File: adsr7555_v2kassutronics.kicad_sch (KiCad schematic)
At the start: 47 parts, among them J1 Power, J2 GateIn, J5 Atn Out, J6 Output, Q1 3904, Q2 3904, Q3 3904, Q4 3904, SW1 SW_Push, U1 7555, U2 TL074

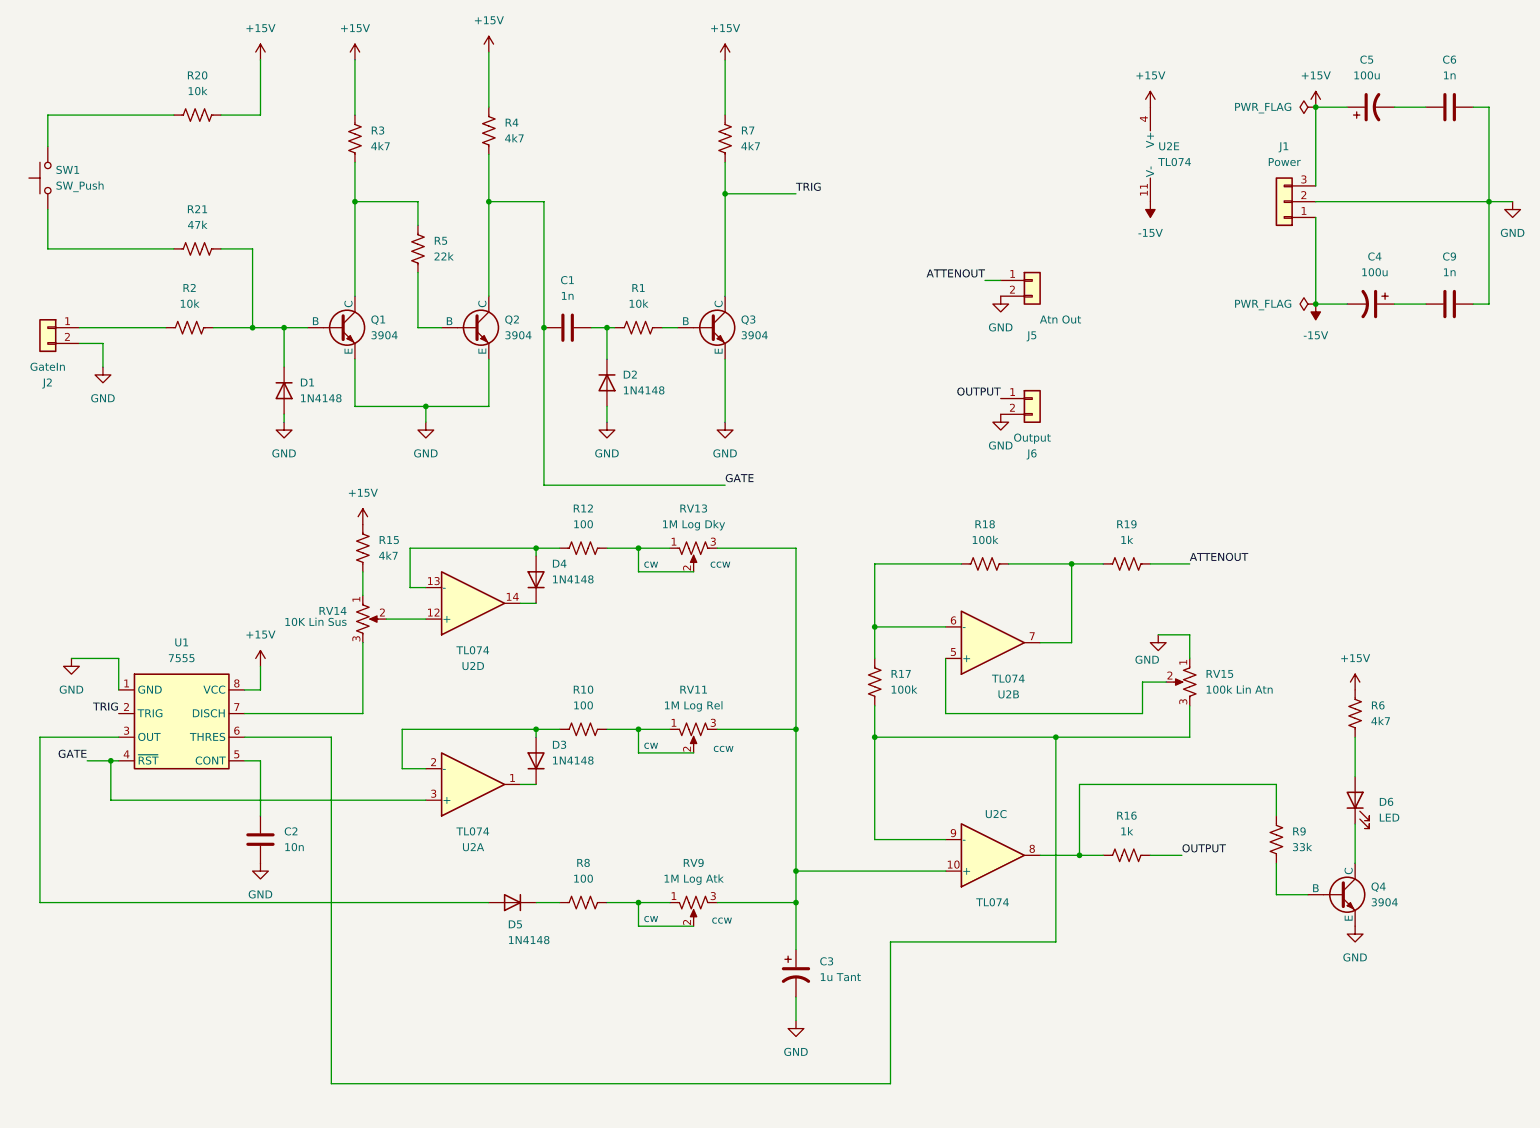
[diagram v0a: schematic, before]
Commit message: archived v1 to jail. Redo for v2
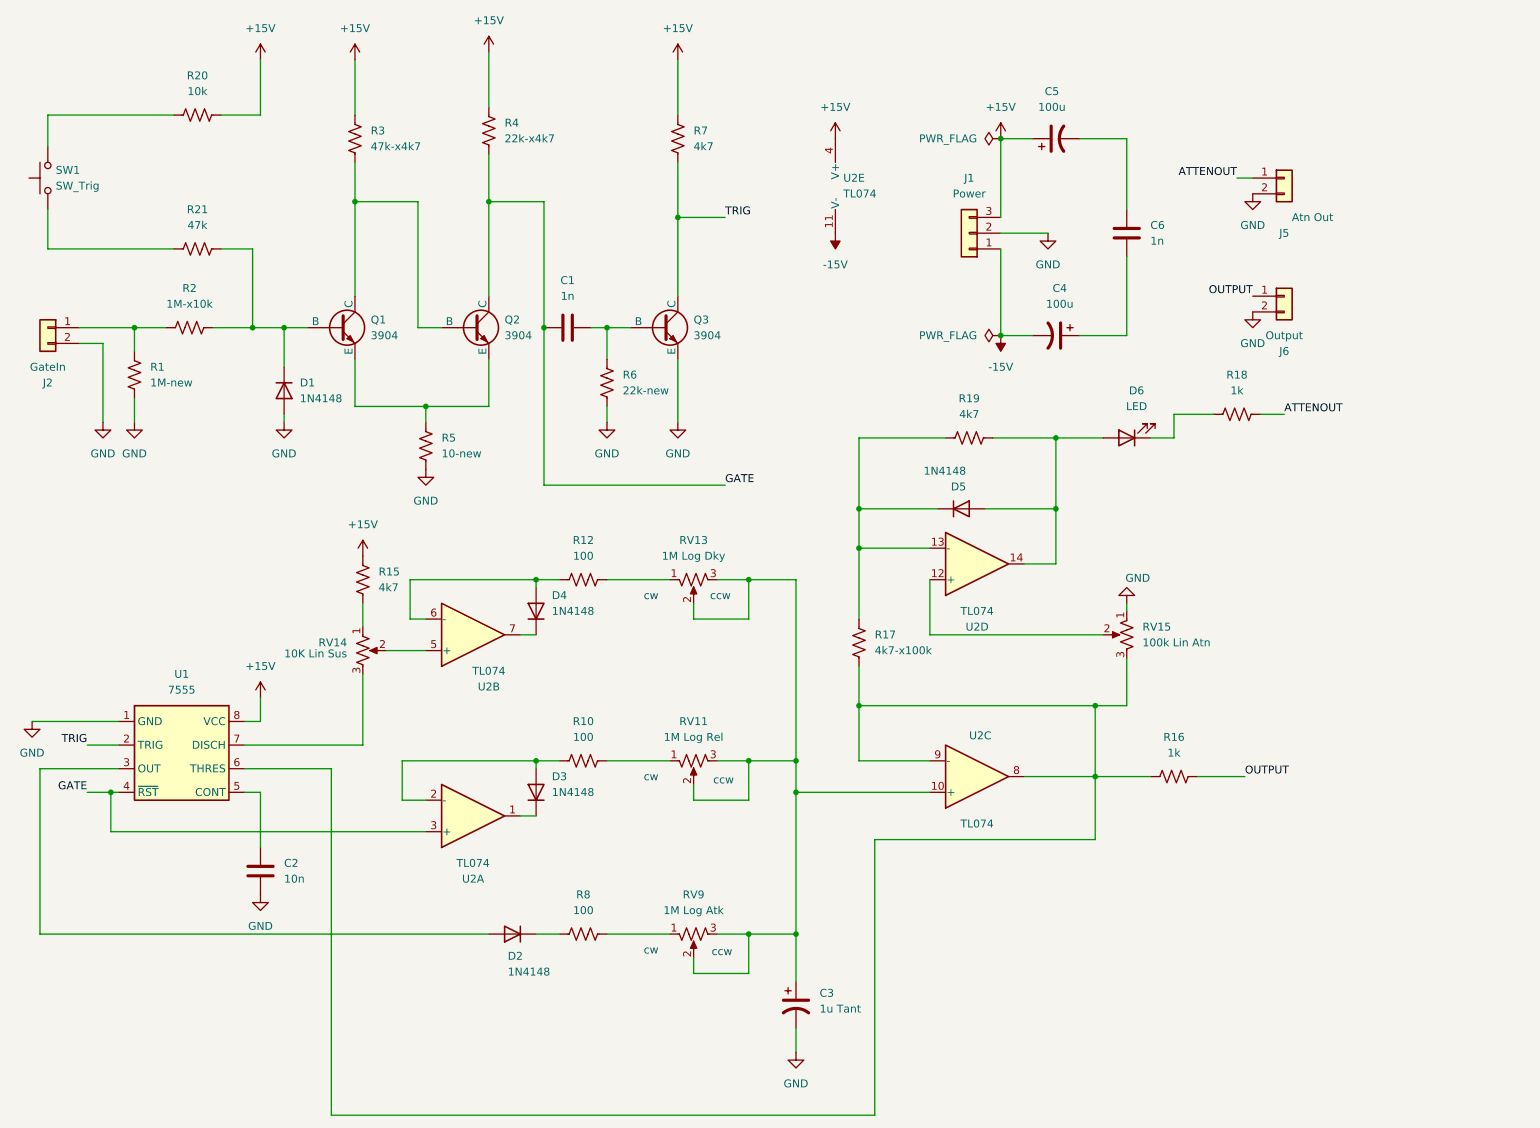
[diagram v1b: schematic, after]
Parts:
- removed C9: 1n, Capacitor_THT:C_Disc_D4.7mm_W2.5mm_P5.00mm, symbol Device:C
- removed D2: 1N4148, Diode_THT:D_DO-35_SOD27_P7.62mm_Horizontal, symbol Diode:1N4148
- removed Q4: 3904, Package_TO_SOT_THT:TO-92L_Inline_Wide, symbol Simulation_SPICE:NPN
- removed R6: 4k7, Resistor_THT:R_Axial_DIN0204_L3.6mm_D1.6mm_P7.62mm_Horizontal, symbol Device:R_US
- removed R9: 33k, Resistor_THT:R_Axial_DIN0204_L3.6mm_D1.6mm_P7.62mm_Horizontal, symbol Device:R_US
- added D5: 1N4148, Diode_THT:D_DO-35_SOD27_P7.62mm_Horizontal, symbol Diode:1N4148
- added R1: 1M-new, Resistor_THT:R_Axial_DIN0204_L3.6mm_D1.6mm_P7.62mm_Horizontal, symbol Device:R_US
- R17: value 100k -> 4k7-x100k
- R19: renamed from R18; value 100k -> 4k7
- R2: value 10k -> 1M-x10k
- R3: value 4k7 -> 47k-x4k7
- R4: value 4k7 -> 22k-x4k7
- R5: value 22k -> 10-new
- R6: renamed from R1; value 10k -> 22k-new
- SW1: value SW_Push -> SW_Trig
- renumbered D5 to D2, R19 to R18
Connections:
- net GND: now also R5.1, R6.1, R1.1; no longer C6.2, Q1.3 (E), Q2.3 (E)
- net at R17.1, RV15.3, U1.6 (THRES)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: now also R16.2, U2.8
- net at RV15.2: now also U2.12 (+); no longer U2.5 (+)
- net at D6.1 (K): now also R18.2
- net at R10.2, RV11.1: no longer RV11.2
- net at C3.1, RV11.3, RV13.3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: now also RV11.2, RV13.2, RV9.2
- net at Q1.1 (C), R3.1: now also Q2.2 (B); no longer R5.2
- net at C1.2: now also Q3.2 (B), R6.2; no longer R6.1
- net at C5.2: now also C6.2; no longer C6.1
- net at RV14.2: now also U2.5 (+); no longer U2.12 (+)
- net at D4.2 (A), R12.1: now also U2.6 (-); no longer U2.13 (-)
- net at U2.14: now also D6.2 (A), R19.1, D5.2 (A); no longer D4.1 (K)
- net at R17.2, R19.2: now also U2.13 (-), D5.1 (K); no longer U2.6 (-)
- net at J2.1 (Pin_1), R2.1: now also R1.2
- net at R12.2, RV13.1: no longer RV13.2
- net at R8.2, RV9.1: no longer RV9.2
- net at C4.1: now also C6.1
- new net: Q1.3 (E), Q2.3 (E), R5.2
- new net: D4.1 (K), U2.7
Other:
- moved on the sheet: C2, C3, C4, C5, D2, D3, D4, D6, J1, J5, J6, Q3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

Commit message: added pdfs for sch and pcb
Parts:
- removed RV15: 100k Lin Atn, Potentiometer_THT:Potentiometer_Bourns_3296W_Vertical, symbol Device:R_Potentiometer_US
- R7: value 4k7 -> 22k-x4k7
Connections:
- net GND: now also U2.12 (+)
- net THR: now reaches R16.2, R17.1, U1.6 (THRES), U2.8, U2.9 (-)
- net ATTENOUT renamed INVOUT
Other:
- title: Kassutronics Precision ADSR -> Kassutronics Precision ADSR V2

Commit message: revised SCH from Bergman
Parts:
- R1: value 1M-new -> 1M
- R17: value 4k7-x100k -> 4k7
- R3: value 47k-x4k7 -> 47k
- R4, R7: value 22k-x4k7 -> 22k
- R5: value 10-new -> 10
- R6: value 22k-new -> 22k
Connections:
- net +15V: now also C6.2; no longer J1.3 (Pin_3)
- net -15V: now also C6.1; no longer J1.1 (Pin_1)
- net at C5.2: now also J1.3 (Pin_3); no longer C6.2
- net at C4.1: now also J1.1 (Pin_1); no longer C6.1
- net INVOUT: no longer names the net of J5.1 (Pin_1), R18.1
- net OUTPUT: no longer names the net of J6.1 (Pin_1), R16.1
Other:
- moved on the sheet: C4, C5, C6, J1, J5, J6, U2E

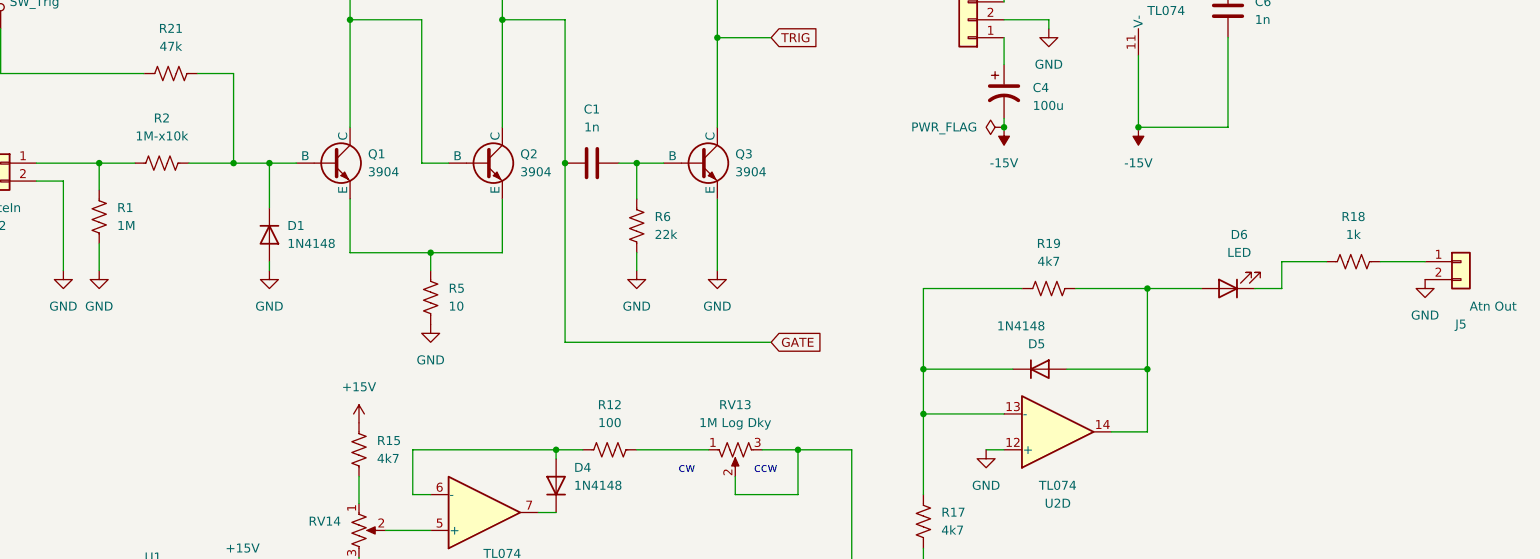
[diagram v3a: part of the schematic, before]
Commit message: modified wiring on U2D
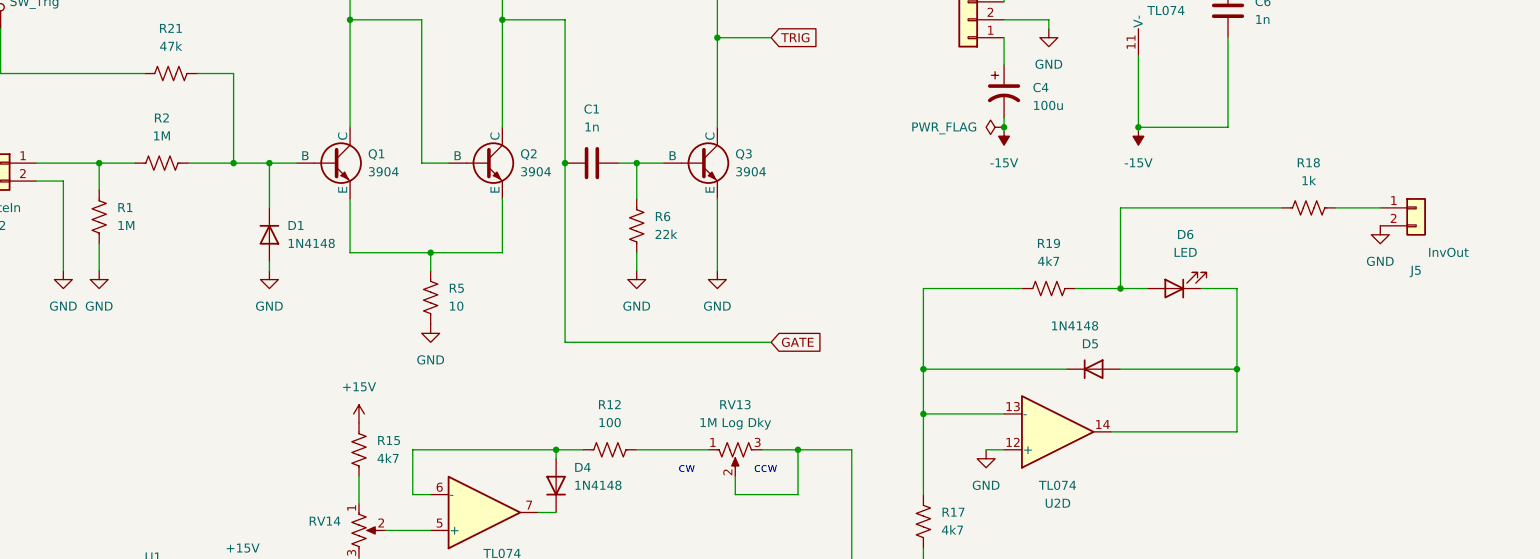
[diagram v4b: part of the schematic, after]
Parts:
- J5: value Atn Out -> InvOut
- R2: value 1M-x10k -> 1M
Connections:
- net at D5.2 (A), U2.14: now also D6.1 (K); no longer D6.2 (A), R19.1
- net at R18.2: now also D6.2 (A), R19.1; no longer D6.1 (K)
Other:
- moved on the sheet: D5, D6, J5, R18
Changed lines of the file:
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@@
 	)
 	(junction
-		(at 181.61 92.71)
-		(diameter 0)
-		(color 0 0 0 0)
-	)
-	(junction
 		(at 80.01 76.2)
 		(diameter 0)
@@
 	)
 	(junction
-		(at 97.79 104.14)
+		(at 194.31 92.71)
 		(diameter 0)
 		(color 0 0 0 0)
 	)
 	(junction
-		(at 90.17 43.18)
+		(at 97.79 104.14)
 		(diameter 0)
 		(color 0 0 0 0)
 	)
 	(junction
-		(at 181.61 81.28)
+		(at 90.17 43.18)
 		(diameter 0)
 		(color 0 0 0 0)
@@
 	)
 	(junction
+		(at 177.8 81.28)
+		(diameter 0)
+		(color 0 0 0 0)
+	)
+	(junction
 		(at 139.7 138.43)
 		(diameter 0)
@@
 	(wire
 		(pts
-			(xy 181.61 81.28) (xy 189.23 81.28)
-		)
-		(stroke
-			(width 0)
-			(type default)
-		)
-	)
-	(wire
-		(pts
-			(xy 196.85 81.28) (xy 200.66 81.28)
+			(xy 177.8 69.85) (xy 200.66 69.85)
 		)
 		(stroke
@@
 	(wire
 		(pts
-			(xy 161.29 57.15) (xy 161.29 58.42)
+			(xy 177.8 81.28) (xy 181.61 81.28)
 		)
 		(stroke
@@
 	(wire
 		(pts
-			(xy 50.8 127) (xy 53.34 127)
+			(xy 161.29 57.15) (xy 161.29 58.42)
 		)
 		(stroke
@@
 	(wire
 		(pts
-			(xy 24.13 66.04) (xy 27.94 66.04)
+			(xy 50.8 127) (xy 53.34 127)
 		)
 		(stroke
@@
 	(wire
 		(pts
-			(xy 52.07 63.5) (xy 57.15 63.5)
+			(xy 24.13 66.04) (xy 27.94 66.04)
 		)
 		(stroke
@@
 	(wire
 		(pts
-			(xy 97.79 133.35) (xy 97.79 134.62)
+			(xy 52.07 63.5) (xy 57.15 63.5)
 		)
 		(stroke
@@
 	(wire
 		(pts
-			(xy 139.7 133.35) (xy 139.7 138.43)
+			(xy 97.79 133.35) (xy 97.79 134.62)
 		)
 		(stroke
@@
 	(wire
 		(pts
-			(xy 200.66 81.28) (xy 200.66 77.47)
+			(xy 139.7 133.35) (xy 139.7 138.43)
 		)
 		(stroke
@@
 	(wire
 		(pts
-			(xy 149.86 92.71) (xy 162.56 92.71)
+			(xy 149.86 92.71) (xy 170.18 92.71)
 		)
 		(stroke
@@
 	(wire
 		(pts
-			(xy 181.61 92.71) (xy 181.61 101.6)
-		)
-		(stroke
-			(width 0)
-			(type default)
-		)
-	)
-	(wire
-		(pts
 			(xy 33.02 63.5) (xy 38.1 63.5)
 		)
@@
 	(wire
 		(pts
-			(xy 214.63 77.47) (xy 220.98 77.47)
+			(xy 208.28 69.85) (xy 214.63 69.85)
 		)
 		(stroke
@@
 	(wire
 		(pts
-			(xy 181.61 81.28) (xy 181.61 92.71)
-		)
-		(stroke
-			(width 0)
-			(type default)
-		)
-	)
-	(wire
-		(pts
 			(xy 52.07 50.8) (xy 52.07 63.5)
 		)
@@
 	(wire
 		(pts
-			(xy 123.19 137.16) (xy 123.19 139.7)
+			(xy 177.8 69.85) (xy 177.8 81.28)
 		)
 		(stroke
@@
 	(wire
 		(pts
-			(xy 132.08 133.35) (xy 139.7 133.35)
+			(xy 123.19 137.16) (xy 123.19 139.7)
 		)
 		(stroke
@@
 	(wire
 		(pts
-			(xy 120.65 45.72) (xy 120.65 58.42)
+			(xy 132.08 133.35) (xy 139.7 133.35)
 		)
 		(stroke
@@
 	(wire
 		(pts
-			(xy 171.45 81.28) (xy 181.61 81.28)
+			(xy 120.65 45.72) (xy 120.65 58.42)
 		)
 		(stroke
@@
 	(wire
 		(pts
-			(xy 200.66 77.47) (xy 207.01 77.47)
+			(xy 171.45 81.28) (xy 177.8 81.28)
 		)
 		(stroke
@@
 	(wire
 		(pts
-			(xy 170.18 92.71) (xy 181.61 92.71)
+			(xy 177.8 92.71) (xy 194.31 92.71)
 		)
 		(stroke
@@
 	(wire
 		(pts
+			(xy 194.31 92.71) (xy 194.31 101.6)
+		)
+		(stroke
+			(width 0)
+			(type default)
+		)
+	)
+	(wire
+		(pts
 			(xy 29.21 138.43) (xy 30.48 138.43)
 		)
@@
 	(wire
 		(pts
-			(xy 176.53 101.6) (xy 181.61 101.6)
+			(xy 176.53 101.6) (xy 194.31 101.6)
 		)
 		(stroke
@@
 	(wire
 		(pts
+			(xy 194.31 81.28) (xy 194.31 92.71)
+		)
+		(stroke
+			(width 0)
+			(type default)
+		)
+	)
+	(wire
+		(pts
 			(xy 187.96 135.89) (xy 187.96 144.78)
 		)
@@
 	(wire
 		(pts
+			(xy 189.23 81.28) (xy 194.31 81.28)
+		)
+		(stroke
+			(width 0)
+			(type default)
+		)
+	)
+	(wire
+		(pts
 			(xy 90.17 76.2) (xy 90.17 68.58)
 		)
@@
 	(symbol
 		(lib_id "power:GND")
-		(at 220.98 80.01 0)
+		(at 214.63 72.39 0)
 		(unit 1)
 		(body_style 1)
@@
 		(fields_autoplaced yes)
 		(property "Reference" "#PWR024"
-			(at 220.98 86.36 0)
+			(at 214.63 78.74 0)
 			(hide yes)
 			(show_name no)
@@
 		)
 		(property "Value" "GND"
-			(at 220.98 85.09 0)
+			(at 214.63 77.47 0)
 			(show_name no)
 			(do_not_autoplace no)
@@
 		)
 		(property "Footprint" ""
-			(at 220.98 80.01 0)
+			(at 214.63 72.39 0)
 			(hide yes)
 			(show_name no)
@@
 		)
 		(property "Datasheet" ""
-			(at 220.98 80.01 0)
+			(at 214.63 72.39 0)
 			(hide yes)
 			(show_name no)
@@
 		)
 		(property "Description" "Power symbol creates a global label with name \"GND\" , ground"
-			(at 220.98 80.01 0)
+			(at 214.63 72.39 0)
 			(hide yes)
 			(show_name no)
@@
 	(symbol
 		(lib_id "Device:LED")
-		(at 193.04 81.28 180)
+		(at 185.42 81.28 180)
 		(unit 1)
 		(body_style 1)
@@
 		(fields_autoplaced yes)
 		(property "Reference" "D6"
-			(at 194.6275 73.66 0)
+			(at 187.0075 73.66 0)
 			(show_name no)
 			(do_not_autoplace no)
@@
 		)
 		(property "Value" "LED"
-			(at 194.6275 76.2 0)
+			(at 187.0075 76.2 0)
 			(show_name no)
 			(do_not_autoplace no)
@@
 		)
 		(property "Footprint" "Connector_Molex:Molex_KK-254_AE-6410-02A_1x02_P2.54mm_Vertical"
-			(at 193.04 81.28 0)
+			(at 185.42 81.28 0)
 			(hide yes)
 			(show_name no)
@@
 		)
 		(property "Datasheet" ""
-			(at 193.04 81.28 0)
+			(at 185.42 81.28 0)
 			(hide yes)
 			(show_name no)
@@
 		)
 		(property "Description" "Light emitting diode"
-			(at 193.04 81.28 0)
+			(at 185.42 81.28 0)
 			(hide yes)
 			(show_name no)
@@
 		)
 		(property "Sim.Pins" "1=K 2=A"
-			(at 193.04 81.28 0)
+			(at 185.42 81.28 0)
 			(hide yes)
 			(show_name no)
@@
 	(symbol
 		(lib_id "Device:R_US")
-		(at 210.82 77.47 270)
+		(at 204.47 69.85 270)
 		(unit 1)
 		(body_style 1)
@@
 		(fields_autoplaced yes)
 		(property "Reference" "R18"
-			(at 210.82 71.12 90)
+			(at 204.47 63.5 90)
 			(show_name no)
 			(do_not_autoplace no)
@@
 		)
 		(property "Value" "1k"
-			(at 210.82 73.66 90)
+			(at 204.47 66.04 90)
 			(show_name no)
 			(do_not_autoplace no)
@@
 		)
 		(property "Footprint" "Resistor_THT:R_Axial_DIN0204_L3.6mm_D1.6mm_P7.62mm_Horizontal"
-			(at 210.566 78.486 90)
+			(at 204.216 70.866 90)
 			(hide yes)
 			(show_name no)
@@
 		)
 		(property "Datasheet" ""
-			(at 210.82 77.47 0)
+			(at 204.47 69.85 0)
 			(hide yes)
 			(show_name no)
@@
 		)
 		(property "Description" "Resistor, US symbol"
-			(at 210.82 77.47 0)
+			(at 204.47 69.85 0)
 			(hide yes)
 			(show_name no)
@@
 	(symbol
 		(lib_id "Connector_Generic:Conn_01x02")
-		(at 226.06 77.47 0)
+		(at 219.71 69.85 0)
 		(unit 1)
 		(body_style 1)
@@
 		(dnp no)
 		(property "Reference" "J5"
-			(at 226.06 86.36 0)
+			(at 219.71 78.74 0)
 			(show_name no)
 			(do_not_autoplace no)
@@
 			)
 		)
-		(property "Value" "Atn Out"
-			(at 230.632 83.82 0)
+		(property "Value" "InvOut"
+			(at 224.282 76.2 0)
 			(show_name no)
 			(do_not_autoplace no)
@@
 		)
 		(property "Footprint" "Connector_Molex:Molex_KK-254_AE-6410-02A_1x02_P2.54mm_Vertical"
-			(at 226.06 77.47 0)
+			(at 219.71 69.85 0)
 			(hide yes)
 			(show_name no)
@@
 		)
 		(property "Datasheet" ""
-			(at 226.06 77.47 0)
+			(at 219.71 69.85 0)
 			(hide yes)
 			(show_name no)
@@
 		)
 		(property "Description" "Generic connector, single row, 01x02, script generated (kicad-library-utils/schlib/autogen/connector/)"
-			(at 226.06 77.47 0)
+			(at 219.71 69.85 0)
 			(hide yes)
 			(show_name no)
@@
 			)
 		)
-		(property "Value" "1M-x10k"
+		(property "Value" "1M"
 			(at 41.91 59.69 90)
 			(show_name no)
@@
 	(symbol
 		(lib_id "Diode:1N4148")
-		(at 166.37 92.71 0)
+		(at 173.99 92.71 0)
 		(unit 1)
 		(body_style 1)
@@
 		(dnp no)
 		(property "Reference" "D5"
-			(at 167.132 89.154 0)
+			(at 174.752 89.154 0)
 			(show_name no)
 			(do_not_autoplace no)
@@
 		)
 		(property "Value" "1N4148"
-			(at 167.132 86.614 0)
+			(at 174.752 86.614 0)
 			(show_name no)
 			(do_not_autoplace no)
@@
 		)
 		(property "Footprint" "Diode_THT:D_DO-35_SOD27_P7.62mm_Horizontal"
-			(at 166.37 92.71 0)
+			(at 173.99 92.71 0)
 			(hide yes)
 			(show_name no)
@@
 		)
 		(property "Datasheet" "https://assets.nexperia.com/documents/data-sheet/1N4148_1N4448.pdf"
-			(at 166.37 92.71 0)
+			(at 173.99 92.71 0)
 			(hide yes)
 			(show_name no)
@@
 		)
 		(property "Description" "100V 0.15A standard switching diode, DO-35"
-			(at 166.37 92.71 0)
+			(at 173.99 92.71 0)
 			(hide yes)
 			(show_name no)
@@
 		)
 		(property "Sim.Device" "D"
-			(at 166.37 92.71 0)
+			(at 173.99 92.71 0)
 			(hide yes)
 			(show_name no)
@@
 		)
 		(property "Sim.Pins" "1=K 2=A"
-			(at 166.37 92.71 0)
+			(at 173.99 92.71 0)
 			(hide yes)
 			(show_name no)
